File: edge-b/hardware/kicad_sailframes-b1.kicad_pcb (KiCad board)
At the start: 2 copper layers, 79.5 x 89.3 mm, 78 parts, among them J1 Conn_01x15, J10 I2C_EXP1, J11 I2C_EXP2, J12 I2C_EXP3, J13 GPIO_EXP, J14 UART_DBG, J15 J_AUX, J16 GNSS_DBG, J17 LATCH_DBG, J2 JST_PH_BAT, J3 U.FL, J4 Conn_01x15, J5 MICROSD, J8 BNO085_DIRECT_SOLDER, J9 HOSYOND_3.5_TFT, U1 LC29HEAMD, U2 TP4056, U3 MT3608

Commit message: B1: D6 cyan->blue, finalize JLC assembly BOM
- D6 LED cyan -> blue (C99290, same as D1) + filled its missing LCSC
- BOM finalized with tier-optimized parts (10k=C25804 Basic, TP4056=C16581,
  yellow=C89811, green=C99289, J1/J4=C2932676); deduped designators
  -> bom-jlcpcb-clean.csv (plugin had a duplicate-designator bug)
- NOTE: U_FF1 still C70285 (DCU) in schematic; correct part is
  SN74LVC1G74DCTR / SM8 = C840104 (fixed in JLC order, update schematic next)

Co-Authored-By: Claude Opus 4.8 (1M context) <noreply@anthropic.com>
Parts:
- D6: value CYAN -> BLUE
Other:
- board text added: "JLCJLCJLCJLC"
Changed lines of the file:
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@@
 			)
 		)
-		(property "Value" "CYAN"
+		(property "Value" "BLUE"
 			(at -10.5 -0.5 0)
 			(layer "F.Fab")
@@
 			)
 		)
+		(property "LCSC Part #" "C99290"
+			(at 0 0 0)
+			(unlocked yes)
+			(layer "F.Fab")
+			(hide yes)
+			(effects
+				(font
+					(size 1 1)
+					(thickness 0.15)
+				)
+			)
+		)
 		(property ki_fp_filters "LED* LED_SMD:* LED_THT:*")
 		(sheetname "/")
@@
 			)
 		)
+		(property "LCSC" "C57369"
+			(at 0 0 0)
+			(layer "F.SilkS")
+			(hide yes)
+			(effects
+				(font
+					(size 1.27 1.27)
+					(thickness 0.15)
+				)
+			)
+		)
 		(property ki_fp_filters "Connector*:*_1x??_*")
 		(sheetname "/")
@@
 			)
 		)
-		(attr through_hole exclude_from_pos_files exclude_from_bom dnp)
+		(attr through_hole)
 		(duplicate_pad_numbers_are_jumpers no)
 		(fp_line
@@
 		)
 	)
-	(gr_text "Sailframes.com\nB1.0"
-		(at 133 74 0)
+	(gr_text "JLCJLCJLCJLC"
+		(at 132.5 73.5 0)
+		(layer "F.SilkS")
+		(effects
+			(font
+				(size 1 1)
+				(thickness 0.15)
+			)
+			(justify left bottom)
+		)
+	)
+	(gr_text "Sailframes.com    B1.0"
+		(at 132 71 0)
 		(layer "F.SilkS")
 		(effects
 			(font
 				(size 2 2)
-				(thickness 0.1)
+				(thickness 0.4)
+				(bold yes)
 			)
 			(justify left bottom)

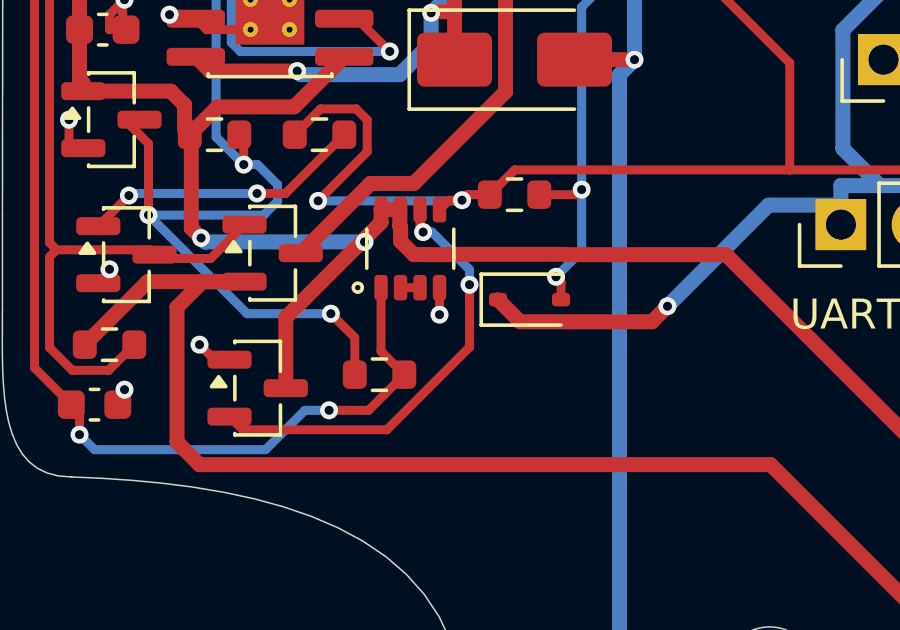
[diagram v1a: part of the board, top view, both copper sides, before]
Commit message: edge-b/B1 hardware: KiCad PCB/schematic update + regenerated production files
- U_FF1 footprint swap: drop the mislabeled SM8 footprint and add the correct
  SN74LVC1G74 TSSOP8 footprint (C458768) to the B1_JLC library
- Updated kicad_sailframes-b1 PCB + schematic
- Regenerated production deliverables: gerbers zip, BOM, IPC netlist, CPL
  positions, and the JLCPCB fab BOM

Co-Authored-By: Claude Opus 4.8 (1M context) <noreply@anthropic.com>
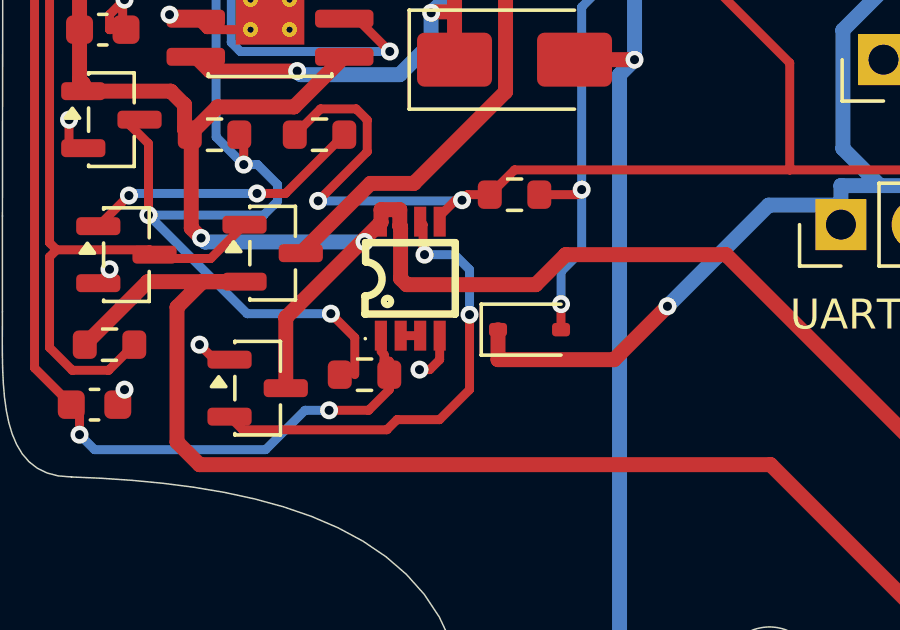
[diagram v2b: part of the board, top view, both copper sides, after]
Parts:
- U_FF1: footprint B1_JLC:VSSOP-8_DCU_2.3x2mm_P0.65mm -> B1_JLC:TSSOP8_74LVC1G74_C458768
- moved D11 1.00 mm to (117.5, 133.0)
- moved U_FF1 1.00 mm to (113.5, 131.3)
- moved R13 0.50 mm to (112.0, 134.5)
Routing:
- net /CLK_DEBOUNCED: track 49.3 -> 46.9 mm
- net /VBAT: track 170.4 -> 171.9 mm
- net /V3V3: track 270.7 -> 271.9 mm
- net /RESET_N: track 14.8 -> 15.9 mm
- net /LATCH_Q_RB: track 53.3 -> 54.1 mm
- net /GND: track 62.2 -> 62.9 mm

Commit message: B1 v0.13: Qi-pad on/off + J5 microSD fix + antenna keepout
Three build-gating fixes for the 30-unit B1 respin, all netlist-verified
(not just DRC-clean — the v0.12 bugs were DRC-clean):

On/off → Qi pad (magnet AND button removed, zero enclosure penetration):
- Delete the magnetic-latch front end: U_HALL1 (DRV5032), U_FF1
  (SN74LVC1G74 FF), U_RST1 (MAX809), R12/R13/C9 debounce, D11 clamp.
- PWR_HOLD = GPIO19 now drives /LATCH_Q through the pre-existing R28
  (value 10k -> 0R so boost EN sees a full 3.3V, not the ~1.9V divider).
  The MCU now holds AND releases its own power.
- Add R30 100k pulldown (default-off), R31/R32 47k/68k V_QI divider ->
  GPIO15 (QI_PRESENT, on-pad ~2.96V). Charge-complete inferred from the
  existing GPIO34 VBAT ADC.
- J17 repurposed to a v0.13 power-debug header (GPIO15/V_QI/LATCH_Q/
  MOSFET_GATE).

J5 microSD pinout fix (was dead on every v0.12 board):
- Correct net->pad: CS->pad2, MOSI->pad3, VDD->pad4, SCK->pad5, GND->pad6,
  MISO->pad7 (card now gets power + clock on the right contacts).
- Drop unused SD_CD (firmware detects via SD.begin/cardType) + delete its
  pull-up R27.

Antenna: ground-pour keepout added under the DevKit antenna (Option 1;
notch/overhang + E1 bench validation still TODO before fab).

Firmware (PWR_HOLD on boot, lift-to-race, charge-complete/low-batt auto-off)
is spec-only in B1_V013_QI_POWER.md, not yet written. Do not fab until the
firmware + antenna overhang + fab-output regen are done.

Co-Authored-By: Claude Opus 4.8 (1M context) <noreply@anthropic.com>
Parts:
- removed C9: 100nF, Capacitor_SMD:C_0603_1608Metric
- removed D11: BAT54, Diode_SMD:D_SOD-323
- removed J15: J_AUX, Connector_PinHeader_2.54mm:PinHeader_1x06_P2.54mm_Vertical
- removed R12: 100k, Resistor_SMD:R_0603_1608Metric
- removed R13, R27: 10k, Resistor_SMD:R_0603_1608Metric
- removed U_FF1: SN74LVC1G74, B1_JLC:TSSOP8_74LVC1G74_C458768
- removed U_HALL1: DRV5032AJDBZR, Package_TO_SOT_SMD:SOT-23
- removed U_RST1: MAX809T, Package_TO_SOT_SMD:SOT-23
- added R30: 100k, Resistor_SMD:R_0603_1608Metric, F.Cu at (117.0, 127.0)
- added R31: 47k, Resistor_SMD:R_0603_1608Metric, F.Cu at (124.0, 124.0)
- added R32: 68k, Resistor_SMD:R_0603_1608Metric, F.Cu at (135.5, 115.5)
- R28: value 10k -> 0
- moved C16 50.5 mm to (112.0, 89.0), turned to 90 degrees
- moved R28 1.00 mm to (117.0, 129.5)
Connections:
- J17 pad 2: /HALL_OUT -> unconnected-(J17-Pin_2-Pad2)
- J17 pad 3: /CLK_DEBOUNCED -> unconnected-(J17-Pin_3-Pad3)
- J5 pad 1: /HSPI_CS -> /V3V3
- J5 pad 2: /HSPI_MOSI -> /HSPI_CS
- J5 pad 3: /HSPI_MISO -> /HSPI_MOSI
- J5 pad 4: /HSPI_SCK -> /V3V3
- J5 pad 5: /V3V3 -> /HSPI_SCK
- J5 pad 7: /SD_CD -> /HSPI_MISO
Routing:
- net /V5_SW: track 183.1 -> 118.8 mm, vias 6 -> 5
- net /CLK_DEBOUNCED: track 46.9 -> 0.00 mm, vias 2 -> 0
- net /HALL_OUT: track 35.7 -> 0.00 mm, vias 3 -> 0
- net /V3V3: track 271.9 -> 246.6 mm, vias 7 -> 6
- net /SD_CD: track 23.5 -> 0.00 mm
- net /HSPI_MISO: track 39.5 -> 59.9 mm, vias 2 -> 1
- net /I2C_SDA: track 101.0 -> 82.7 mm, vias 0 -> 1
- net /I2C_SCL: track 88.6 -> 71.0 mm, vias 1 -> 2
- net /RESET_N: track 15.9 -> 0.00 mm, vias 2 -> 0
- net /GPIO15: track 27.7 -> 41.3 mm, vias 1 -> 4
- net /VBAT: track 171.9 -> 159.9 mm
- net /AUX_INT: track 59.2 -> 47.4 mm
- net /GND: track 62.9 -> 74.1 mm, vias 42 -> 43
- net /LATCH_Q_RB: track 54.1 -> 49.6 mm, vias 2 -> 1
- net /V_QI: track 69.6 -> 71.8 mm
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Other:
- board size 79.5 x 89.3 mm -> 79.6 x 89.3 mm
- board text added: "Sailframes.com B1.1"
- board text removed: "Sailframes.com B1.0"
